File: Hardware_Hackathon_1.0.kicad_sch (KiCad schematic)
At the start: 11 parts, among them J2 Conn_01x04, Q1 BC817, SW1 SW_Push_SPDT

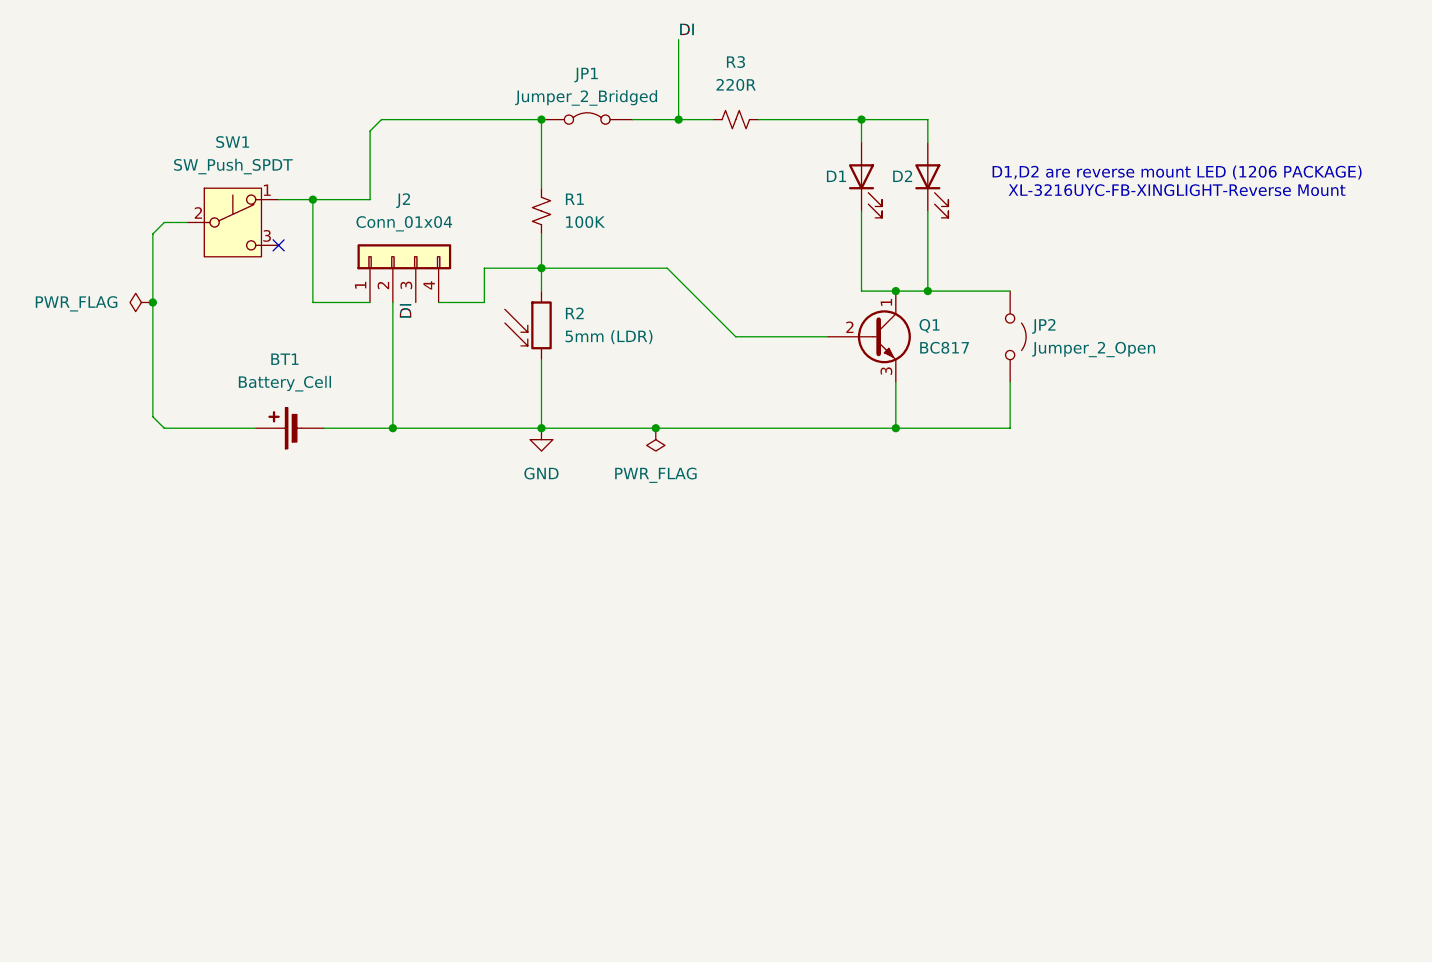
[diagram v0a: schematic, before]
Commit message: fixed BC817 symbol and footprint pin reversal
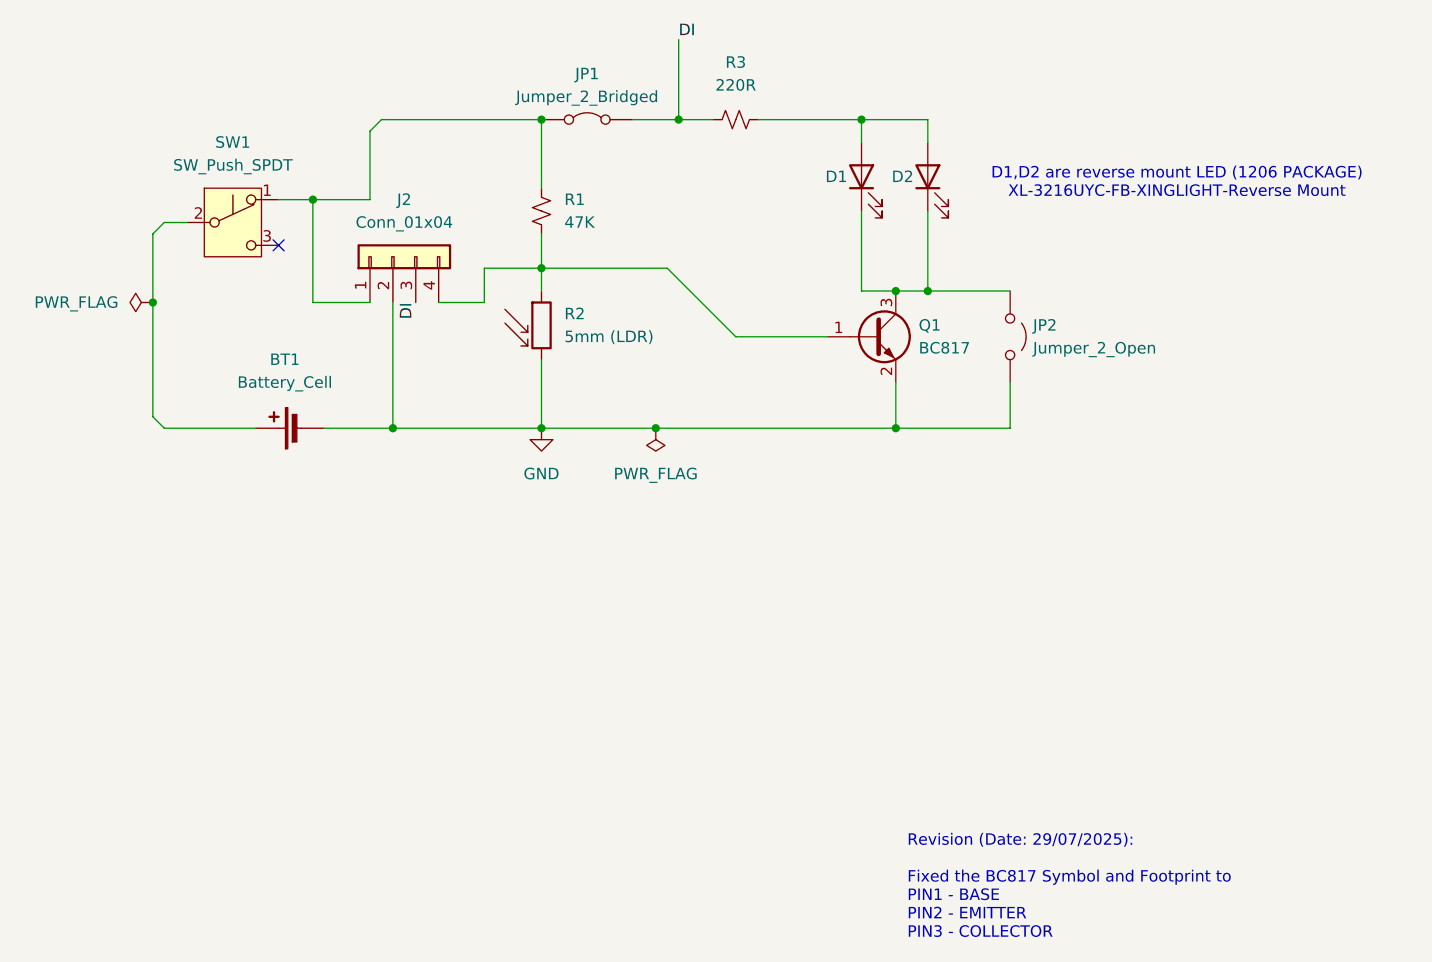
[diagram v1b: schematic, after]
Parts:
- removed Q1: BC817, Package_TO_SOT_SMD:TSOT-23, symbol Transistor_BJT:BC547
- added Q1: BC817, Package_TO_SOT_SMD:SOT-23, symbol Transistor_BJT:BC817
- R1: value 100K -> 47K
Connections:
- net GND: now also Q1.2 (E)
- net at J2.4 (Pin_4), R1.1, R2.1: now also Q1.1 (B)
- net at D1.1 (K), D2.1 (K), JP2.1 (A): now also Q1.3 (C)
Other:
- note added: "Revision (Date: 29/07/2025): Fixed the BC817 Symbol and Footprint to PIN1 - BASE PIN2 - EMITTER PIN3 - COLLECTOR"
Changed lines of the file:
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@@
+		)
+	)
+	(text "Revision (Date: 29/07/2025):\n\nFixed the BC817 Symbol and Footprint to\nPIN1 - BASE\nPIN2 - EMITTER\nPIN3 - COLLECTOR"
+		(exclude_from_sim no)
+		(at 176.53 157.734 0)
+		(effects
+			(font
+				(size 1.27 1.27)
+			)
+			(justify left)
 		)
 	)
@@
 	)
 	(junction
-		(at 175.26 91.44)
-		(diameter 0)
-		(color 0 0 0 0)
-	)
-	(junction
 		(at 151.13 72.39)
 		(diameter 0)
@@
 	)
 	(junction
+		(at 175.26 91.44)
+		(diameter 0)
+		(color 0 0 0 0)
+	)
+	(junction
 		(at 135.89 72.39)
 		(diameter 0)
@@
 	(wire
 		(pts
+			(xy 175.26 91.44) (xy 178.816 91.44)
+		)
+		(stroke
+			(width 0)
+			(type default)
+		)
+	)
+	(wire
+		(pts
 			(xy 178.816 82.55) (xy 178.816 91.44)
 		)
@@
 		(pts
 			(xy 135.89 99.06) (xy 135.89 106.68)
-		)
-		(stroke
-			(width 0)
-			(type default)
-		)
-	)
-	(wire
-		(pts
-			(xy 175.26 91.44) (xy 178.816 91.44)
 		)
 		(stroke
@@
 			)
 			(justify left bottom)
+		)
+	)
+	(symbol
+		(lib_id "Transistor_BJT:BC817")
+		(at 172.72 96.52 0)
+		(unit 1)
+		(exclude_from_sim no)
+		(in_bom yes)
+		(on_board yes)
+		(dnp no)
+		(fields_autoplaced yes)
+		(property "Reference" "Q1"
+			(at 177.8 95.2499 0)
+			(effects
+				(font
+					(size 1.27 1.27)
+				)
+				(justify left)
+			)
+		)
+		(property "Value" "BC817"
+			(at 177.8 97.7899 0)
+			(effects
+				(font
+					(size 1.27 1.27)
+				)
+				(justify left)
+			)
+		)
+		(property "Footprint" "Package_TO_SOT_SMD:SOT-23"
+			(at 177.8 98.425 0)
+			(effects
+				(font
+					(size 1.27 1.27)
+					(italic yes)
+				)
+				(justify left)
+				(hide yes)
+			)
+		)
+		(property "Datasheet" "https://www.onsemi.com/pub/Collateral/BC818-D.pdf"
+			(at 172.72 96.52 0)
+			(effects
+				(font
+					(size 1.27 1.27)
+				)
+				(justify left)
+				(hide yes)
+			)
+		)
+		(property "Description" "0.8A Ic, 45V Vce, NPN Transistor, SOT-23"
+			(at 172.72 96.52 0)
+			(effects
+				(font
+					(size 1.27 1.27)
+				)
+				(hide yes)
+			)
+		)
+		(pin "1"
+		)
+		(pin "3"
+		)
+		(pin "2"
+		)
+		(instances
+			(project ""
+				(path "/1e18e8ab-8efb-4c4e-8c67-d8bddaa41069"
+					(reference "Q1")
+					(unit 1)
+				)
+			)
 		)
 	)
@@
 			)
 		)
-		(property "Value" "100K"
+		(property "Value" "47K"
 			(at 138.43 83.8199 0)
 			(effects
@@
 					(unit 1)
 				)
-			)
-		)
-	)
-	(symbol
-		(lib_id "Transistor_BJT:BC547")
-		(at 172.72 96.52 0)
-		(unit 1)
-		(exclude_from_sim no)
-		(in_bom yes)
-		(on_board yes)
-		(dnp no)
-		(fields_autoplaced yes)
-		(property "Reference" "Q1"
-			(at 177.8 95.2499 0)
-			(effects
-				(font
-					(size 1.27 1.27)
-				)
-				(justify left)
-			)
-		)
-		(property "Value" "BC817"
-			(at 177.8 97.7899 0)
-			(effects
-				(font
-					(size 1.27 1.27)
-				)
-				(justify left)
-			)
-		)
-		(property "Footprint" "Package_TO_SOT_SMD:TSOT-23"
-			(at 177.8 98.425 0)
-			(effects
-				(font
-					(size 1.27 1.27)
-					(italic yes)
-				)
-				(justify left)
-				(hide yes)
-			)
-		)
-		(property "Datasheet" "https://www.onsemi.com/pub/Collateral/BC550-D.pdf"
-			(at 172.72 96.52 0)
-			(effects
-				(font
-					(size 1.27 1.27)
-				)
-				(justify left)
-				(hide yes)
-			)
-		)
-		(property "Description" "0.1A Ic, 45V Vce, Small Signal NPN Transistor, TO-92"
-			(at 172.72 96.52 0)
-			(effects
-				(font
-					(size 1.27 1.27)
-				)
-				(hide yes)
-			)
-		)
-		(property "MANUFACTURER" ""
-			(at 172.72 96.52 0)
-			(effects
-				(font
-					(size 1.27 1.27)
-				)
-				(hide yes)
-			)
-		)
-		(property "MAXIMUM_PACKAGE_HEIGHT" ""
-			(at 172.72 96.52 0)
-			(effects
-				(font
-					(size 1.27 1.27)
-				)
-				(hide yes)
-			)
-		)
-		(property "PARTREV" ""
-			(at 172.72 96.52 0)
-			(effects
-				(font
-					(size 1.27 1.27)
-				)
-				(hide yes)
-			)
-		)
-		(property "STANDARD" ""
-			(at 172.72 96.52 0)
-			(effects
-				(font
-					(size 1.27 1.27)
-				)
-				(hide yes)
-			)
-		)
-		(pin "2"
-		)
-		(pin "3"
-		)
-		(pin "1"
-		)
-		(instances
-			(project "Hardware_Hackathon_1.0"
-				(path "/1e18e8ab-8efb-4c4e-8c67-d8bddaa41069"
-					(reference "Q1")
-					(unit 1)
-				)
